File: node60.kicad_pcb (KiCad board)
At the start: 2 copper layers, 250 x 160 mm, 12 parts, among them J901 74660016R, J902 74660016R, J903 ATM13-2P-BM04, J904 AT13-2P-BM04, J905 AT13-2P-BM04, J906 AT13-2P-BM04, J907 AT13-2P-BM04, J908 AT13-2P-BM04, J909 AT13-2P-BM04, J910 74660016R, J911 74660016R, J912 ATM13-2P-BM04

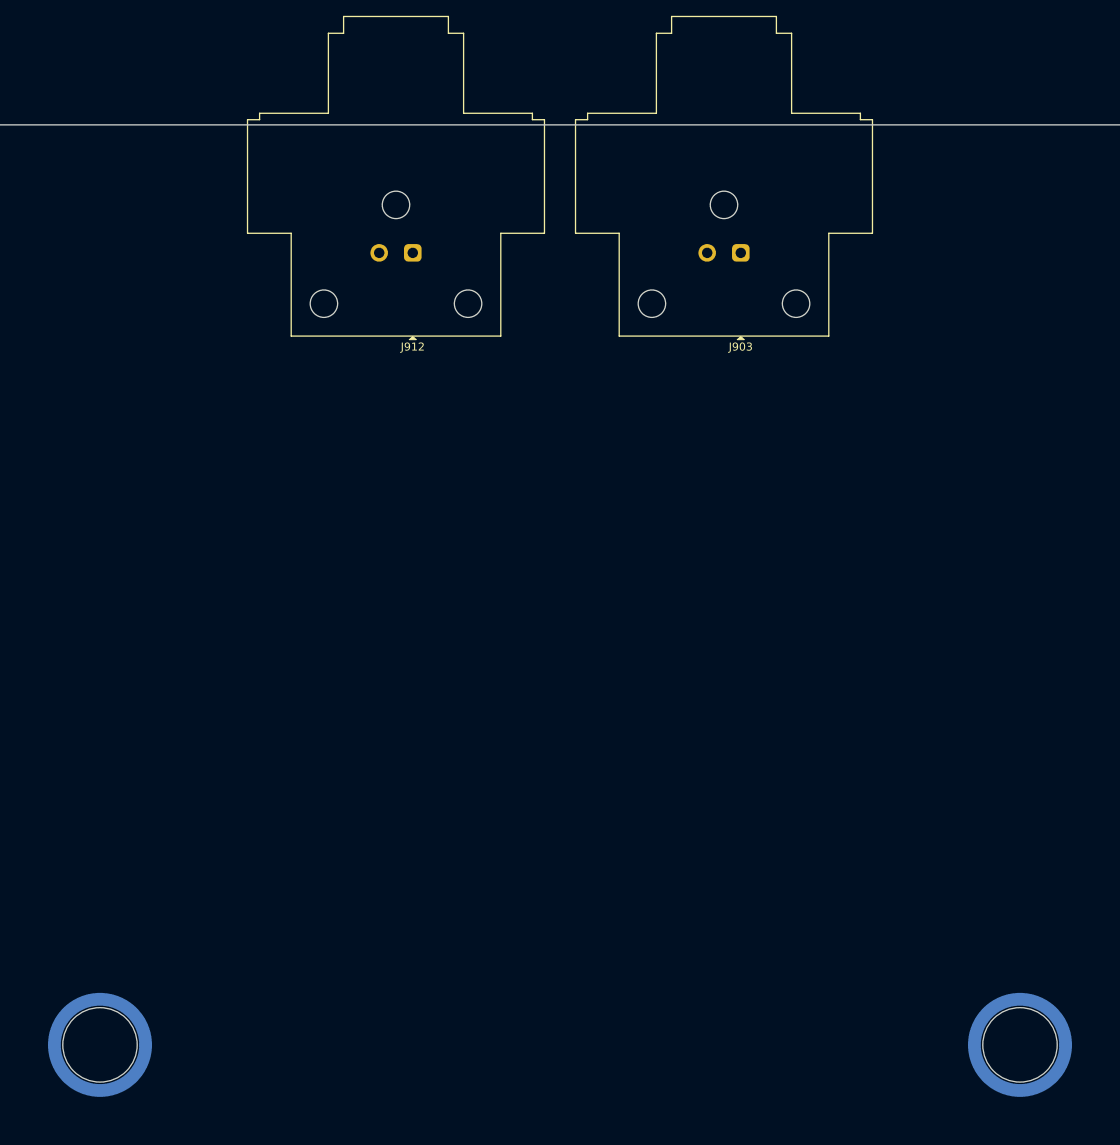
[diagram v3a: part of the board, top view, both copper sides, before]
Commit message: Enclosure: removable north panel for v2/v7; T1S 40 mm; board-fitting check
- check_assembly.py (new): how each version's boards go into the case.
  A header's shroud passes through a closed cutout, so a board slides
  toward its headers' wall; a board with headers on two one-piece walls
  needs a split case. Versions 1 and 3-6 need one.
- Versions 2 and 7 (user, 2026-10-31): the north wall is a separate
  panel. The board is lowered 15.1 mm north, slid south into the
  one-piece front wall, then the panel slides 13.4 mm south onto the
  T1S shrouds. Sliding over its standoffs needs a 15.1 mm keep-out
  strip south of each mounting hole on the underside.
- Versions 2, 4 and 7: J903/J912 40 mm apart (were 41). Version 2's
  battery receptacles J910/J901 move 5 mm north, 50 mm from the front
  edge. node60.kicad_pcb re-placed (version 2); DRC with schematic
  parity is clean. DEC-021 records both.
- Version 8 (candidate only, not an architecture decision): main board
  15.1 mm shorter, notch moved, placeholder mezzanine with a 2.5 mm
  drop, output cutouts 2.5 mm taller.
- Mockup: Assembly slider for versions 2, 7 and 8; the boards and the
  removable panel move as separate parts; follows #vN hash changes.
- Drawing engine 1.3: names removable panels in their face views.
- Docs: Fitting the board column, PCB and mezzanine rows.

Co-Authored-By: Claude Opus 5.5 <noreply@anthropic.com>
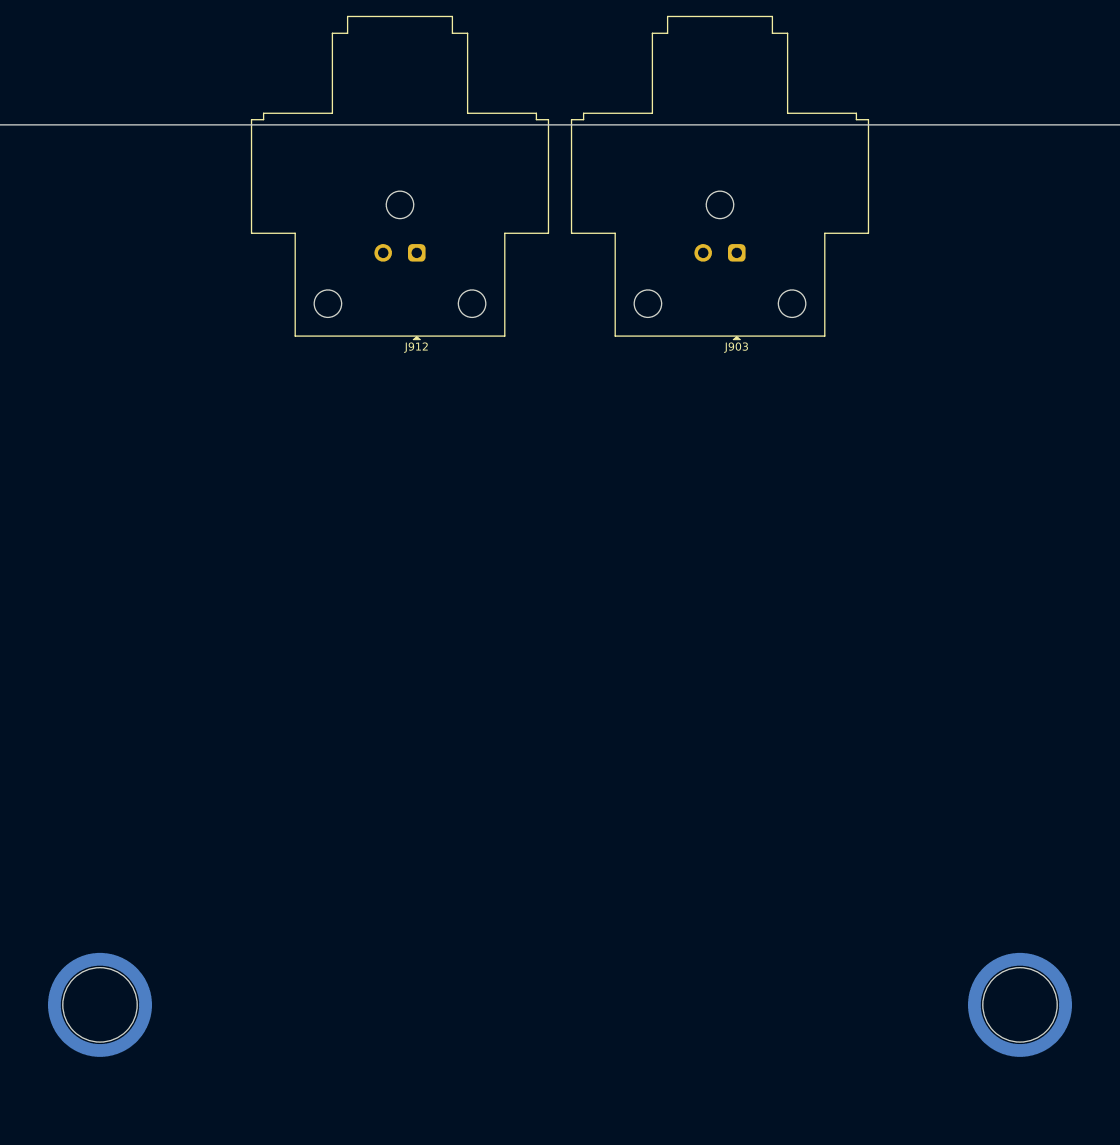
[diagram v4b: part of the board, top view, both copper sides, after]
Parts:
- moved J901 5.00 mm to (212.5, 140.0)
- moved J910 5.00 mm to (97.5, 140.0)
- moved J903 0.50 mm to (177.1, 46.0)
- moved J912 0.50 mm to (137.1, 46.0)
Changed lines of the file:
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@@
 		(locked yes)
 		(layer "F.Cu")
-		(at 177.6 46 180)
+		(at 177.1 46 180)
 		(descr "Amphenol Sine BoardLock ATM13-2P-BMxx 2-pin right-angle PCB receptacle with flange (mates ATM06-2S), 4.20 mm pitch, 3x #4-20 screw bosses; PCB layout and body per drawing ATM13-2P-BMXX rev. A2, https://www.amphenol-sine.com/pdf/datasheet/ATM13-2P-BM04.pdf")
 		(tags "connector Amphenol Sine ATM ATM13 ATM13-2P ATM06-2S BoardLock horizontal right angle sealed automotive")
@@
 		(locked yes)
 		(layer "F.Cu")
-		(at 136.6 46 180)
+		(at 137.1 46 180)
 		(descr "Amphenol Sine BoardLock ATM13-2P-BMxx 2-pin right-angle PCB receptacle with flange (mates ATM06-2S), 4.20 mm pitch, 3x #4-20 screw bosses; PCB layout and body per drawing ATM13-2P-BMXX rev. A2, https://www.amphenol-sine.com/pdf/datasheet/ATM13-2P-BM04.pdf")
 		(tags "connector Amphenol Sine ATM ATM13 ATM13-2P ATM06-2S BoardLock horizontal right angle sealed automotive")
@@
 		(locked yes)
 		(layer "B.Cu")
-		(at 97.5 145)
+		(at 97.5 140)
 		(descr "Würth REDCUBE SMT WP-SMRT, reverse with internal thread, M6, Ø12 flange, Ø9.3 non-plated hole for the Ø9.0 spigot, 85 A (data sheet 74660016 rev. 001.001 p. 1), https://www.we-online.com/components/products/datasheet/74660016.pdf")
 		(tags "REDCUBE SMT power terminal M6 internal thread reverse WP-SMRT 74660016 74660016R")
@@
 		(locked yes)
 		(layer "B.Cu")
-		(at 212.5 145)
+		(at 212.5 140)
 		(descr "Würth REDCUBE SMT WP-SMRT, reverse with internal thread, M6, Ø12 flange, Ø9.3 non-plated hole for the Ø9.0 spigot, 85 A (data sheet 74660016 rev. 001.001 p. 1), https://www.we-online.com/components/products/datasheet/74660016.pdf")
 		(tags "REDCUBE SMT power terminal M6 internal thread reverse WP-SMRT 74660016 74660016R")
@@
 	)
 	(gr_rect
-		(start 84.8 132.3)
-		(end 225.2 157.7)
+		(start 84.8 127.3)
+		(end 225.2 152.7)
 		(stroke
 			(width 0.15)
@@
 	)
 	(gr_text "VBAT_IN busbar 25.4 x 3.175 Cu (1/8 x 1 in C110), on top: no parts under it"
-		(at 155 130.3 0)
+		(at 155 125.3 0)
 		(layer "Dwgs.User")
 		(effects

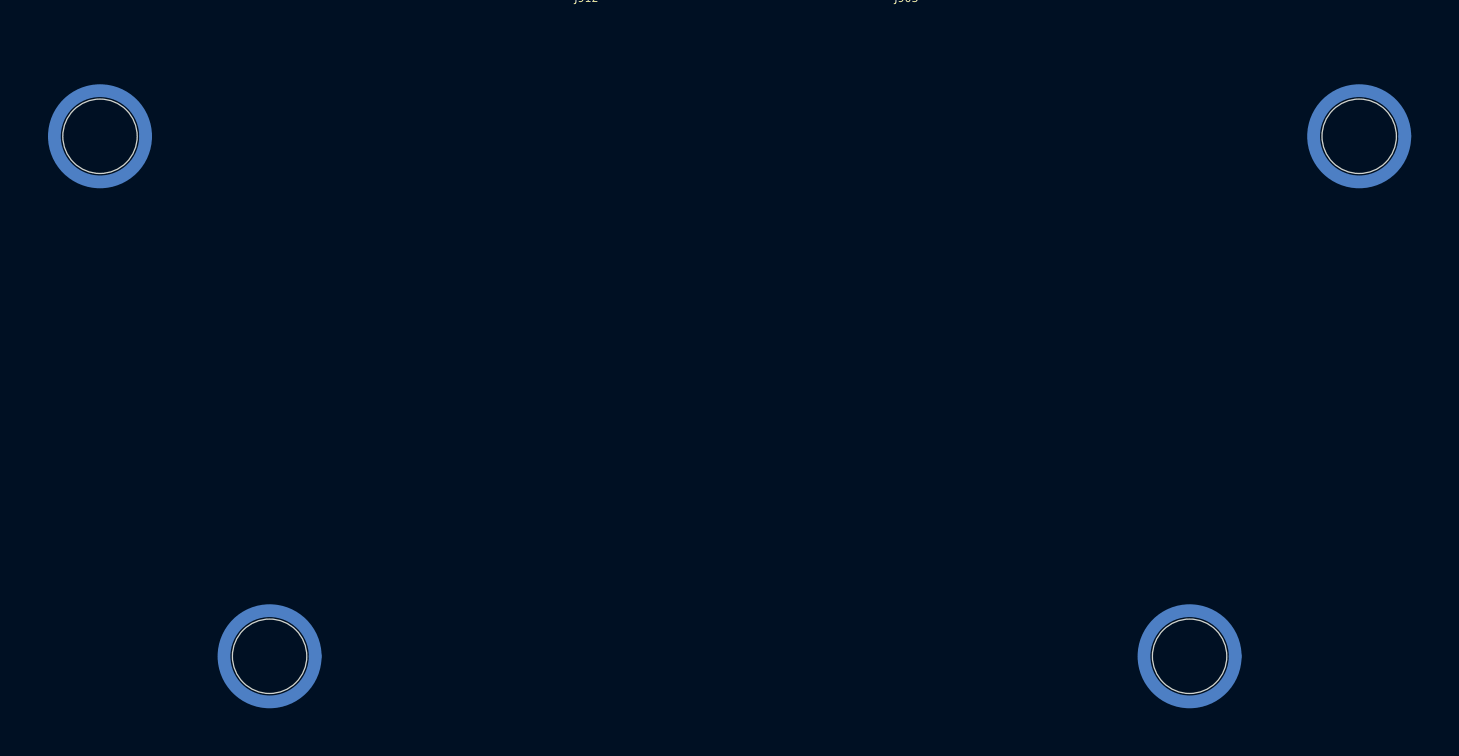
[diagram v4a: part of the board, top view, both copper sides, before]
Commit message: DEC-022: enclosure version 4, press-fit terminals and a flat lid
The user chose enclosure version 4 (2026-10-31): a flat lid simplifies
the mechanical design and seals on one level instead of across the
vertical faces of a step.

- DEC-022 (accepted, Rev B, supersedes DEC-021): Würth REDCUBE
  PRESS-FIT 786202106 terminals (180 A, M6 blind thread) on F.Cu with
  the 1/8" x 1" busbars on the blocks; flat 4 mm machined lid with a
  2.6 mm seat and M4 bosses per SurLok receptacle; board 5 mm off the
  floor; removable north panel. DEC-016's receptacles and pass-through
  stand; its terminal part is replaced.
- Parts: 786202106 selected (4), 74660016R now an alternative (0).
- Schematic: J901, J902, J910, J911 -> 786202106 (same one-pin symbol
  and nets).
- PCB: CURRENT = v4; the four terminals placed as press-fit parts on
  F.Cu. DRC with schematic parity clean; schematic conventions OK.
- Docs: harness page, Rev B list, Enclosure options, GATE-HAR-02,
  CLAUDE.md.

Co-Authored-By: Claude Opus 5.5 <noreply@anthropic.com>
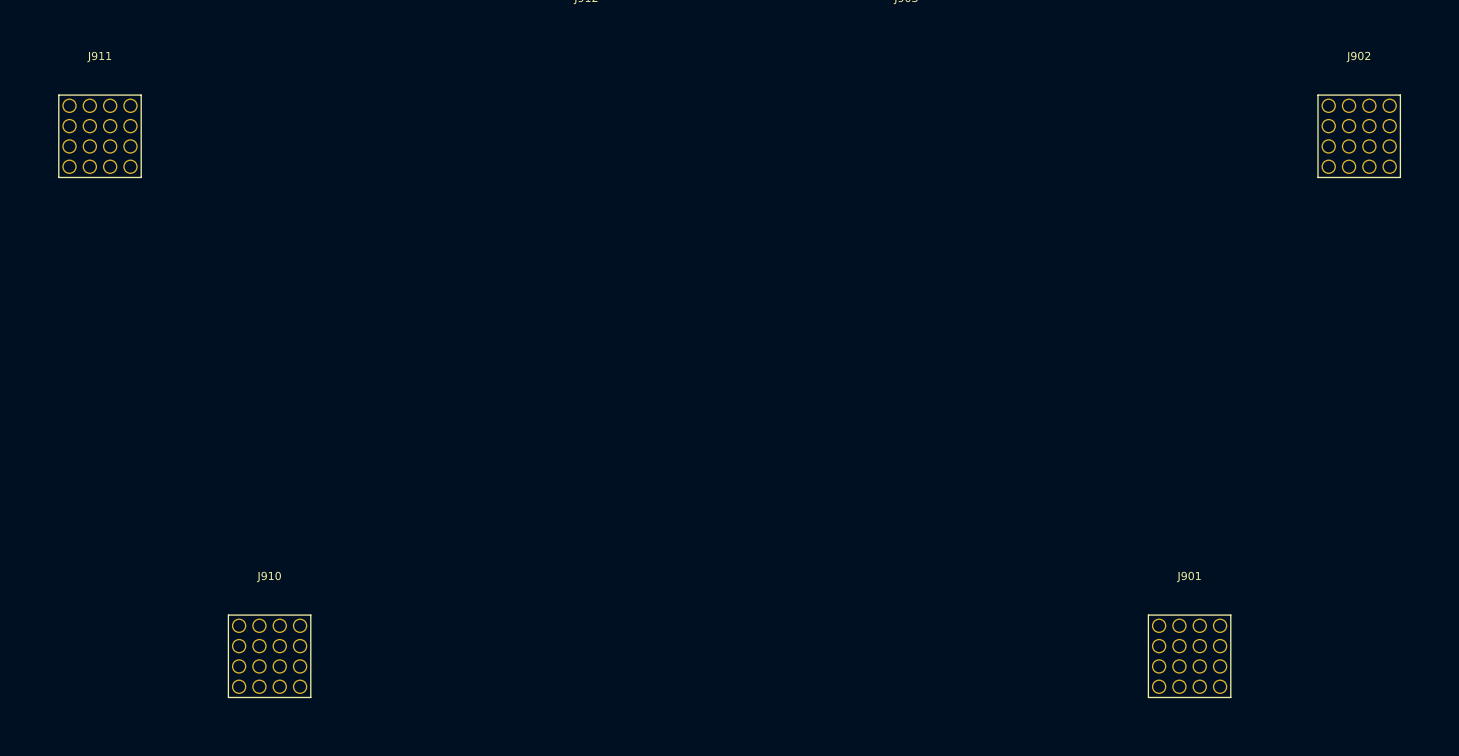
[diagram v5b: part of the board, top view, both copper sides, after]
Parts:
- J901, J902, J910, J911: value 74660016R -> 786202106; footprint DropOut_TerminalBlock_Wuerth:Wuerth_REDCUBE-SMT_WP-SMRT_74660016 -> DropOut_TerminalBlock_Wuerth:Wuerth_REDCUBE-PRESS-FIT_WP-PFIFUA_786202106_PressFit; moved to F.Cu
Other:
- board text added: "GND busbar 25.4 x 3.175 Cu (1/8 x 1 in C110), on the press-fit blocks, 10.5 mm up: parts under it below 9 mm, 4 mm from the blocks"
- board text added: "VBAT_IN busbar 25.4 x 3.175 Cu (1/8 x 1 in C110), on the press-fit blocks, 10.5 mm up: parts under it below 9 mm, 4 mm from the blocks"
- board text removed: "GND busbar 25.4 x 3.175 Cu (1/8 x 1 in C110), on top: no parts under it"
- board text removed: "VBAT_IN busbar 25.4 x 3.175 Cu (1/8 x 1 in C110), on top: no parts under it"
